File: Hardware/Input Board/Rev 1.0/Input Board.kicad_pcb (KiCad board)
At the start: 2 copper layers, 100 x 100 mm, 31 parts, among them J1 6502 Bus, J2 PORT B, J3 Conn_02x08_Odd_Even, J4 SNES Controller Port 1, J5 Keyboard, J6 Mouse, J7 SNES Controller Port 2, U1 65C22, U2 74HC138, U3 74HC595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

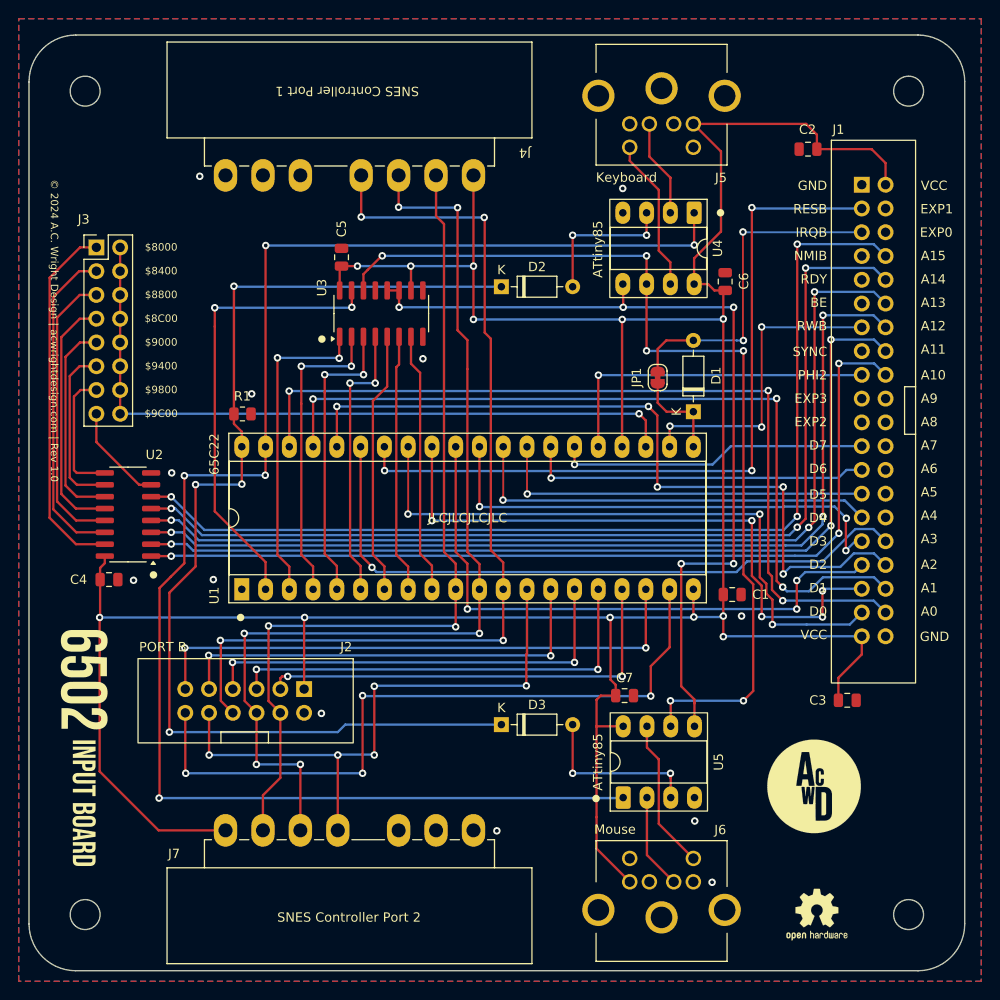
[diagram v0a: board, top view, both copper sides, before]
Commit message: Begin Input Board redesign
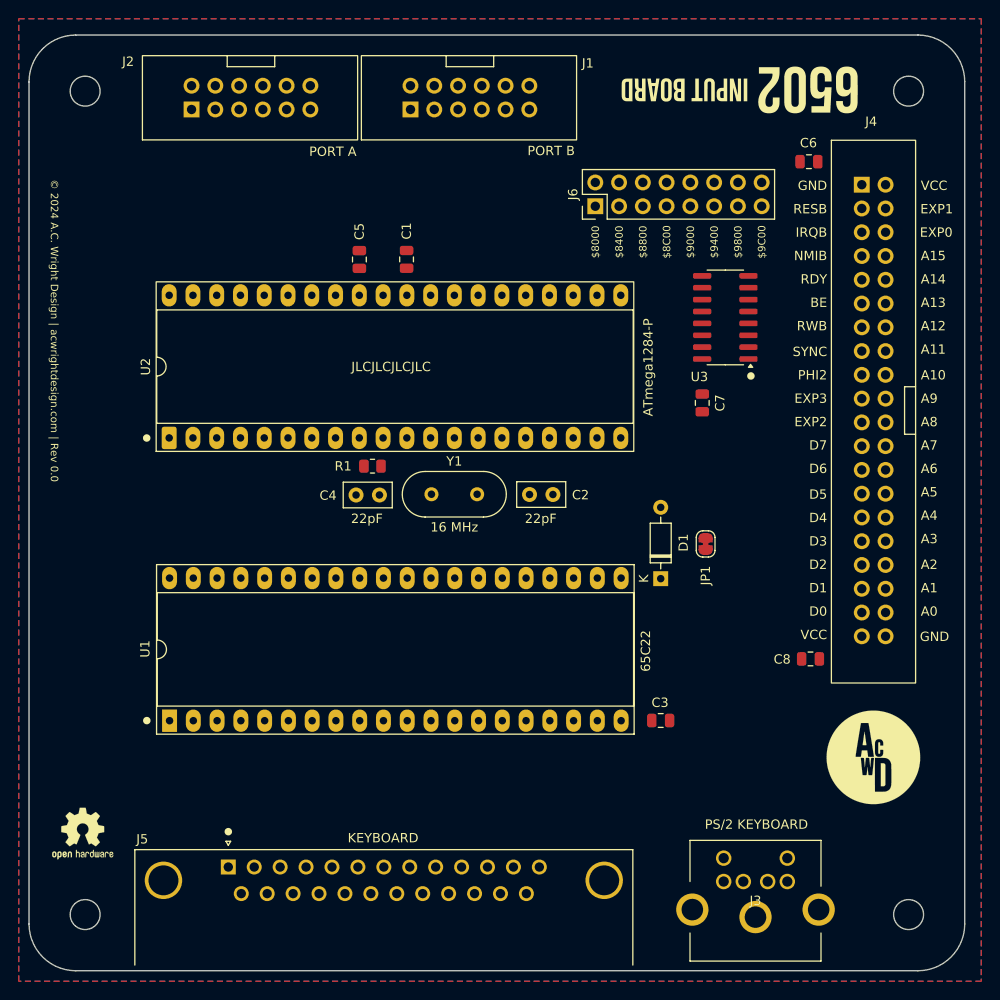
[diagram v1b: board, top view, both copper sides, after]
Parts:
- removed D2, D3: D_Schottky, Diode_THT:D_DO-35_SOD27_P7.62mm_Horizontal
- removed J7: SNES Controller Port 2, 6502 Parts:SNES Controller Port
- removed U4, U5: ATtiny85, Package_DIP:DIP-8_W7.62mm_Socket_LongPads
- added C8: 100nF, Capacitor_SMD:C_0805_2012Metric, F.Cu at (173.5, 116.7)
- added Y1: 16 MHz, Crystal:Crystal_HC49-U_Vertical, F.Cu at (133.0, 99.1)
- C2, C4: value 100nF -> 22pF; footprint Capacitor_SMD:C_0805_2012Metric -> Capacitor_THT:C_Disc_D5.0mm_W2.5mm_P2.50mm
- J1: value 6502 Bus -> PORT B; footprint 6502 Parts:6502 Bus Connector -> 6502 Parts:6502 GPIO Connector
- J2: value PORT B -> PORT A
- J3: value Conn_02x08_Odd_Even -> PS/2 KEYBOARD; footprint Connector_PinHeader_2.54mm:PinHeader_2x08_P2.54mm_Vertical -> 6502 Parts:KMDGX-6S-BS
- J4: value SNES Controller Port 1 -> 6502 Bus; footprint 6502 Parts:SNES Controller Port -> 6502 Parts:6502 Bus Connector
- J5: value Keyboard -> KEYBOARD; footprint 6502 Parts:KMDGX-6S-BS -> Connector_Dsub:DSUB-25_Pins_Horizontal_P2.77x2.84mm_EdgePinOffset7.70mm_Housed_MountingHolesOffset9.12mm
- J6: value Mouse -> Conn_02x08_Odd_Even; footprint 6502 Parts:KMDGX-6S-BS -> Connector_PinHeader_2.54mm:PinHeader_2x08_P2.54mm_Vertical
- R1: value 10k -> 1K
- U2: value 74HC138 -> ATmega1284-P; footprint Package_SO:SOIC-16_3.9x9.9mm_P1.27mm -> Package_DIP:DIP-40_W15.24mm_Socket_LongPads
- U3: value 74HC595 -> 74HC138
- moved G*** 99.8 mm to (158.6, 55.9), turned to 180 degrees
- moved J3 98.7 mm to (168.9, 140.5), turned to 180 degrees
- moved J5 91.3 mm to (111.3, 138.9)
- moved REF** 78.9 mm to (95.7, 135.3)
- moved J6 72.7 mm to (150.5, 68.3), turned to 90 degrees
- moved J2 63.1 mm to (107.4, 58.0), turned to 90 degrees
- moved C1 49.9 mm to (130.3, 74.0), turned to -90 degrees
- moved J1 48.9 mm to (130.8, 58.0), turned to 90 degrees
- moved C2 47.4 mm to (143.5, 99.1), turned to 0 degrees
- moved J4 41.5 mm to (179.0, 66.0), turned to 0 degrees
- moved U3 36.8 mm to (164.4, 80.2), turned to 180 degrees
- moved C7 32.4 mm to (161.9, 89.3), turned to -90 degrees
- moved C4 30.3 mm to (127.5, 99.2), turned to 180 degrees
- moved C3 20.1 mm to (157.5, 123.3)
- moved JP1 18.5 mm to (162.3, 104.4)
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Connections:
- C2 pad 1: VCC -> Net-(U2-XTAL1)
- C4 pad 1: VCC -> Net-(U2-XTAL2)
- C5 pad 1: VCC -> GND
- C5 pad 2: GND -> Net-(U2-AREF)
- J1 pad 1: GND -> VCC
- J1 pad 10: A14 -> PB3
- J1 pad 11: /BE -> CB1
- J1 pad 12: A13 -> CB2
- J1 pad 2: VCC -> GND
- J1 pad 3: RESB -> PB7
- J1 pad 4: /EXP1 -> PB0
- J1 pad 5: IRQB -> PB6
- J1 pad 6: /EXP0 -> PB1
- J1 pad 7: /NMIB -> PB5
- J1 pad 8: A15 -> PB2
- J1 pad 9: /RDY -> PB4
- J2 pad 10: PB3 -> PA3
- J2 pad 11: CB1 -> CA1
- J2 pad 12: CB2 -> CA2
- J2 pad 3: PB7 -> PA7
- J2 pad 4: PB0 -> PA0
- J2 pad 5: PB6 -> PA6
- J2 pad 6: PB1 -> PA1
- J2 pad 7: PB5 -> PA5
- J2 pad 8: PB2 -> PA2
- J2 pad 9: PB4 -> PA4
- J3 pad 1: /$8000 -> PS2DATA
- J3 pad 2: CSB -> unconnected-(J3-Pad2)
- J3 pad 3: /$8400 -> GND
- J3 pad 4: CSB -> VCC
- J3 pad 5: /$8800 -> PS2CLK
- J3 pad 6: CSB -> unconnected-(J3-Pad6)
- J4 pad 1: VCC -> GND
- J4 pad 2: PB0 -> VCC
- J4 pad 3: PB1 -> RESB
- J4 pad 4: PB2 -> /EXP1
- J4 pad 5: unconnected-(J4-NC-Pad5) -> IRQB
- J4 pad 6: unconnected-(J4-NC-Pad6) -> /EXP0
- J4 pad 7: GND -> /NMIB
- J5 pad 1: KBD_DATA -> VCC
- J5 pad 2: unconnected-(J5-Pad2) -> PA0
- J5 pad 3: GND -> PA2
- J5 pad 4: VCC -> PA4
- J5 pad 5: KBD_CLK -> PA6
- J5 pad 6: unconnected-(J5-Pad6) -> CA2
- J6 pad 1: MS_DATA -> /$8000
- J6 pad 2: unconnected-(J6-Pad2) -> CSB
- J6 pad 3: GND -> /$8400
- J6 pad 4: VCC -> CSB
- J6 pad 5: MS_CLK -> /$8800
- J6 pad 6: unconnected-(J6-Pad6) -> CSB
- R1 pad 1: Net-(D2-K) -> VCC
- R1 pad 2: GND -> Net-(U2-~{RESET})
- U1 pad 39: CS -> CA2
- U1 pad 40: Net-(D2-K) -> CA1
- U2 pad 1: A10 -> PB0
- U2 pad 10: /$9400 -> VCC
- U2 pad 11: /$9000 -> GND
- U2 pad 12: /$8C00 -> Net-(U2-XTAL2)
- U2 pad 13: /$8800 -> Net-(U2-XTAL1)
- U2 pad 14: /$8400 -> CA1
- U2 pad 15: /$8000 -> CA2
- U2 pad 16: VCC -> PS2CLK
- U2 pad 2: A11 -> PB1
- U2 pad 3: A12 -> PB2
- U2 pad 4: A13 -> PB3
- U2 pad 5: A14 -> PB4
- U2 pad 6: A15 -> PB5
- U2 pad 7: /$9C00 -> PB6
- U2 pad 8: GND -> PB7
- U2 pad 9: /$9800 -> Net-(U2-~{RESET})
- U3 pad 1: PA1 -> A10
- U3 pad 10: VCC -> /$9400
- U3 pad 11: CLK -> /$9000
- U3 pad 12: CLK -> /$8C00
- U3 pad 13: GND -> /$8800
- U3 pad 14: DATA -> /$8400
- U3 pad 15: PA0 -> /$8000
- U3 pad 2: PA2 -> A11
- U3 pad 3: PA3 -> A12
- U3 pad 4: PA4 -> A13
- U3 pad 5: PA5 -> A14
- U3 pad 6: PA6 -> A15
- U3 pad 7: PA7 -> /$9C00
- U3 pad 9: unconnected-(U3-QH&apos;-Pad9) -> /$9800
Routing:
- net VCC: track 334.8 -> 0.00 mm, vias 12 -> 0
- net CS: track 167.7 -> 0.00 mm, vias 5 -> 0
- net Net-(D2-K): track 118.5 -> 0.00 mm, vias 4 -> 0
- net A15: track 110.2 -> 0.00 mm, vias 3 -> 0
- net A14: track 107.7 -> 0.00 mm, vias 3 -> 0
- net PB1: track 107.6 -> 0.00 mm, vias 6 -> 0
- net A13: track 105.3 -> 0.00 mm, vias 3 -> 0
- net A12: track 102.9 -> 0.00 mm, vias 3 -> 0
- net PB2: track 102.2 -> 0.00 mm, vias 4 -> 0
- net DATA: track 102.1 -> 0.00 mm, vias 6 -> 0
- net A11: track 100.3 -> 0.00 mm, vias 3 -> 0
- net A10: track 98.2 -> 0.00 mm, vias 3 -> 0
- net PB0: track 92.3 -> 0.00 mm, vias 2 -> 0
- net CLK: track 92.3 -> 0.00 mm, vias 5 -> 0
- net A0: track 91.8 -> 0.00 mm, vias 3 -> 0
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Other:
- board text added: "© 2024 A.C. Wright Design | acwrightdesign.com | Rev 0.0"
- board text removed: "© 2024 A.C. Wright Design | acwrightdesign.com | Rev 1.0"

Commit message: Input Board PCB
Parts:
- moved JP1 1.67 mm to (160.6, 104.3)
- moved C8 0.16 mm to (173.4, 116.7)
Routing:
- net VCC: track 0.00 -> 332.1 mm, vias 0 -> 14
- net PB3: track 0.00 -> 174.0 mm, vias 0 -> 12
- net PB1: track 0.00 -> 165.6 mm, vias 0 -> 8
- net PB2: track 0.00 -> 162.8 mm, vias 0 -> 7
- net PB0: track 0.00 -> 158.2 mm, vias 0 -> 6
- net CA2: track 0.00 -> 149.7 mm, vias 0 -> 5
- net PB4: track 0.00 -> 140.6 mm, vias 0 -> 6
- net CA1: track 0.00 -> 139.1 mm, vias 0 -> 7
- net PB7: track 0.00 -> 134.0 mm, vias 0 -> 6
- net PB5: track 0.00 -> 132.8 mm, vias 0 -> 10
- net PB6: track 0.00 -> 131.5 mm, vias 0 -> 6
- net CB2: track 0.00 -> 114.0 mm, vias 0 -> 4
- net PA7: track 0.00 -> 113.8 mm, vias 0 -> 6
- net CB1: track 0.00 -> 107.9 mm, vias 0 -> 4
- net RESB: track 0.00 -> 98.0 mm, vias 0 -> 5
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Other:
- board text added: "© 2024 A.C. Wright Design | acwrightdesign.com | Rev 1.0"
- board text removed: "© 2024 A.C. Wright Design | acwrightdesign.com | Rev 0.0"
